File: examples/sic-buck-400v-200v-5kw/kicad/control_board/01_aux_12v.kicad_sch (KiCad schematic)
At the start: 15 parts, among them J1 12 V in, U1 TPS26400PWPR

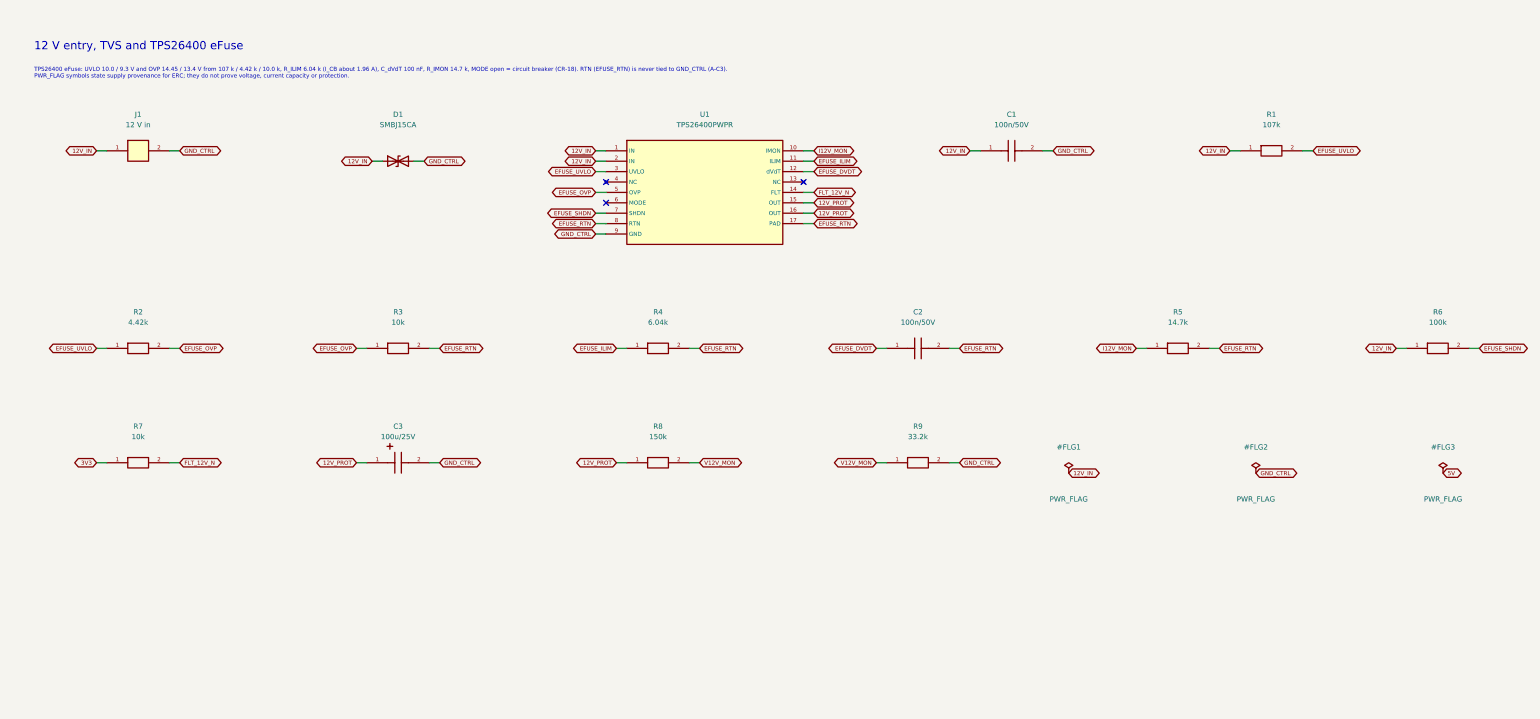
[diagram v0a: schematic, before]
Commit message: feat(v2.1): example regenerated - wired schematics, both boards routed with the upgraded router, exports, crops, validation
Schematics (wired style, gates passed): ERC 0 on both projects (power 20261012T075113Z-erc-df18ce6e,
control 20261012T075120Z-erc-7a14cacb); netlist (ref,pad)->net exact vs the model and vs the frozen V2
netlists with equal net names; .kicad_dru / net_settings identical to the legacy generation; stub
global labels 648 -> 7 (power) and 667 -> 7 (control), wired pin share 0 -> 0.90 / 0.76, junctions,
hierarchical labels and power symbols introduced, continuation sheets removed; readability metrics
V2 vs V2.1 in engineering_checks/schematic_readability_*.

Power board (octilinear simplification + tangent arcs on the V2 search; 8-direction search kept
opt-in after attempt A left 2 connections open): 0 unresolved, DRC 0/0/0 (20261012T090308Z-drc-8fd50803),
segments 4755 -> 2991 + 145 arcs, 90-degree bends 3609 -> 1121, stair runs 382 -> 124, length
5744.6 -> 5545.6 mm, vias 606 = V2, no net longer / more vias / narrower. Control board: 0 unresolved,
DRC 0/0/0 (20261012T084327Z-drc-7f07f983), segments 5995 -> 4262 + 261 arcs, 90-degree bends
4069 -> 1233, stair runs 435 -> 144, length 7055.2 -> 6700.7 mm, vias 798 = V2, 96 nets shorter,
0 longer. FOOTPRINT.SetDNP for DNP parts (schematic parity), beautify anchors bound to off-grid vias
by copper overlap (path_geometry.connected_by_overlap), In2.Cu inner pass styled.

Exports 11/11 per board, renders and layer PDFs refreshed, high-resolution V2/V2.1 crops under
review/crops/, routing_quality_* and v21_validation.{json,md} (nine TASK 7 checks independently
re-derived). verify_sic_buck passed; 338 tests OK (2 skipped).

Co-Authored-By: Claude Fable 5.1 <noreply@anthropic.com>
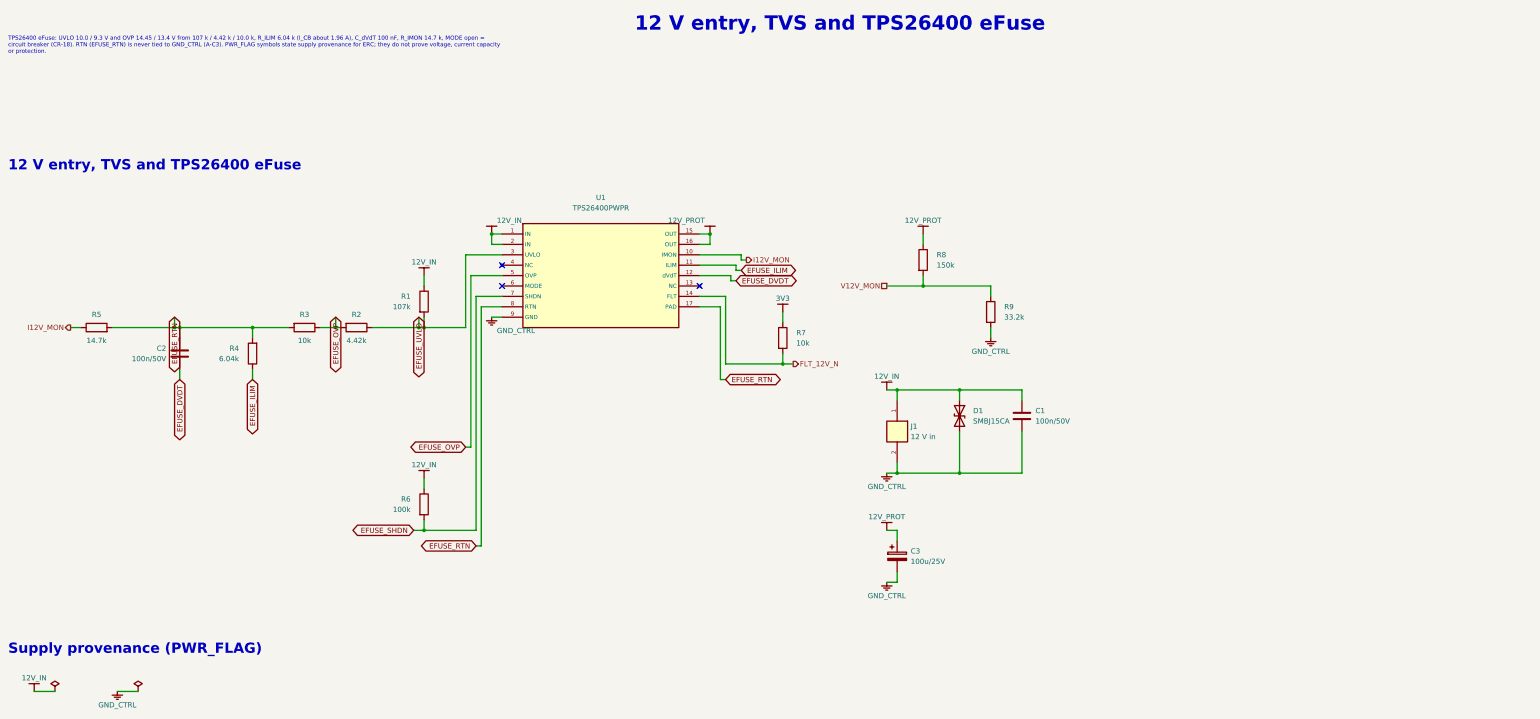
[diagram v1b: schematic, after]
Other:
- note added: "Supply provenance (PWR_FLAG)"
- moved on the sheet: D1, J1, U1
